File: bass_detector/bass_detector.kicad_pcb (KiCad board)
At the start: 2 copper layers, 65 x 65 mm, 27 parts, among them J1 AudioJack3, J2 Screw_Terminal_01x02, SW1 SW_SPST, U1 LM358

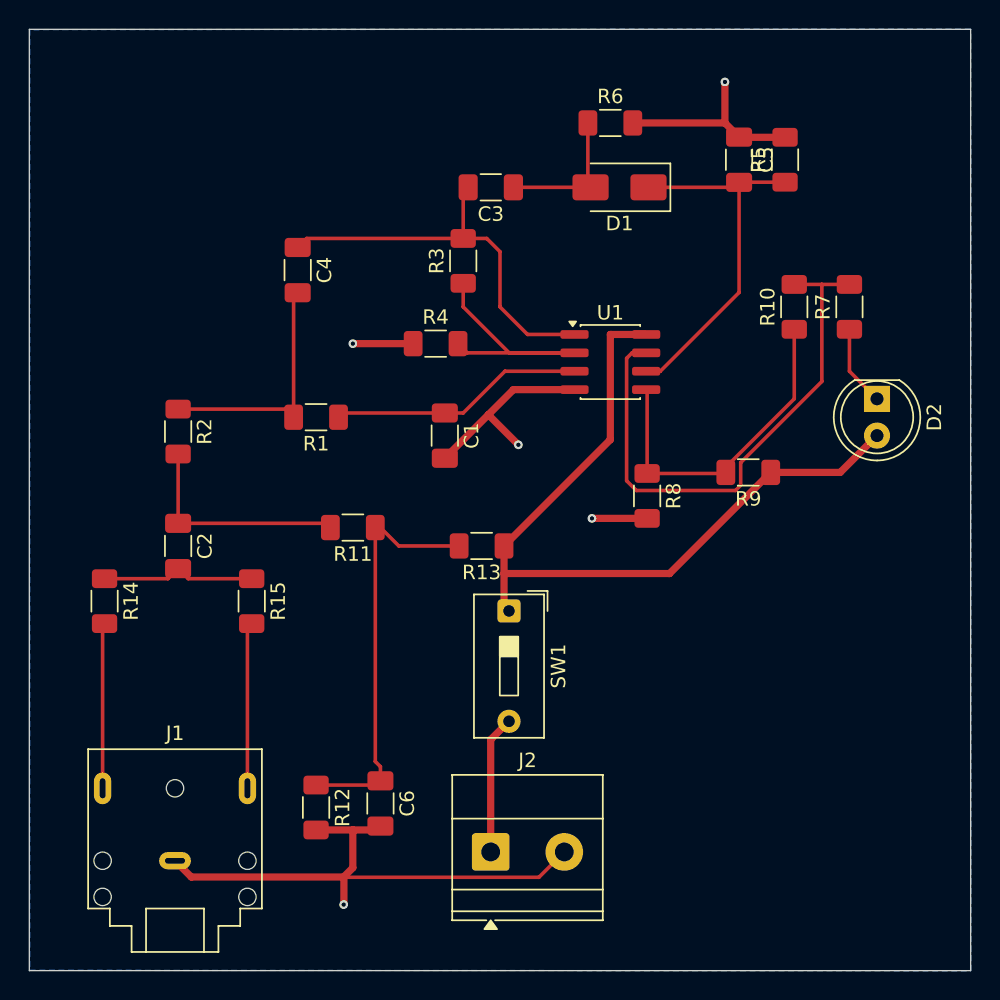
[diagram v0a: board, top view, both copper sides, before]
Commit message: made the pcb smaller, changed the language to be en only
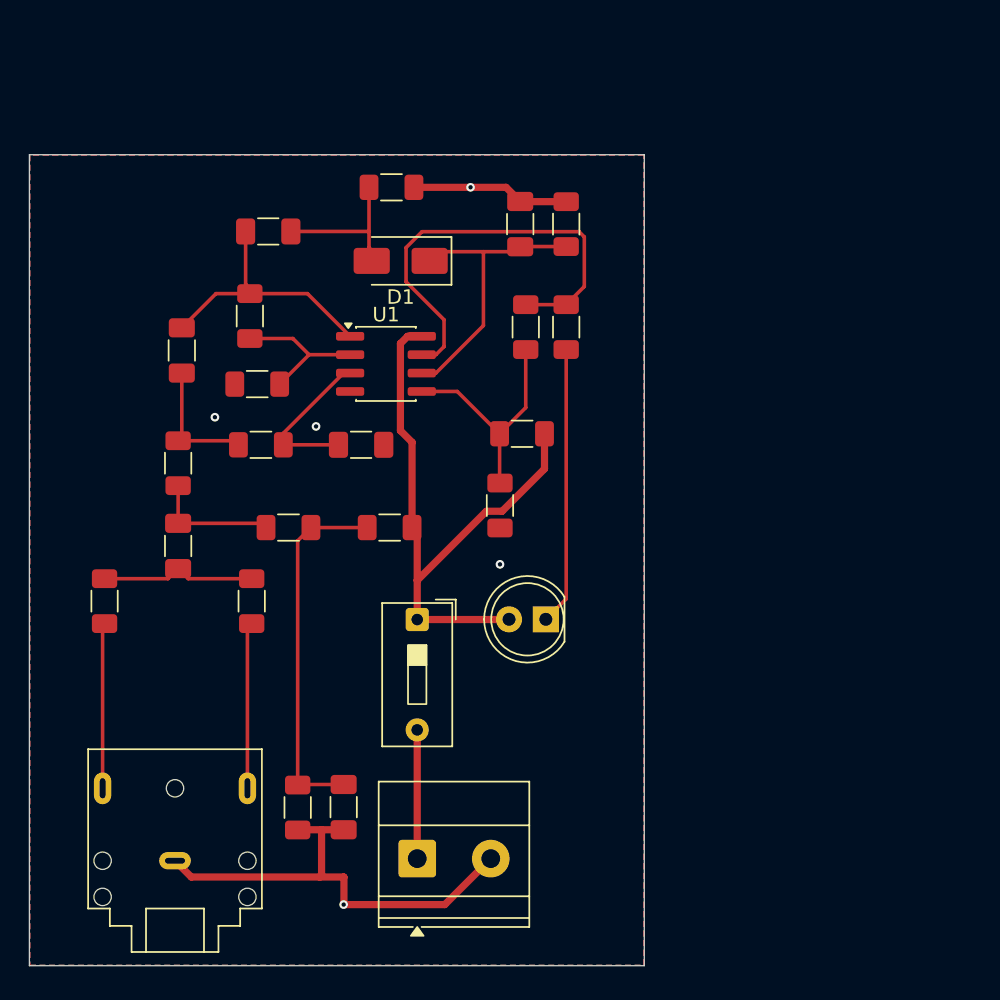
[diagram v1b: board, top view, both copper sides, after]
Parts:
- moved D2 27.5 mm to (153.7, 125.1), turned to 180 degrees
- moved R7 19.6 mm to (155.1, 104.9)
- moved R10 18.6 mm to (152.3, 104.9)
- moved D1 15.9 mm to (143.6, 100.3)
- moved R9 15.8 mm to (152.0, 112.3)
- moved C5 15.8 mm to (151.9, 97.8)
- moved R5 15.8 mm to (155.1, 97.8)
- moved R6 15.8 mm to (143.0, 95.2)
- moved C3 15.7 mm to (134.5, 98.3)
- moved U1 15.5 mm to (142.6, 107.4)
- moved R3 15.2 mm to (133.2, 104.1)
- moved R4 12.6 mm to (133.7, 108.8)
- moved R8 10.2 mm to (150.5, 117.2)
- moved C4 9.74 mm to (128.5, 106.5)
- moved R13 6.48 mm to (142.9, 118.7)
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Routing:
- net GND: track 73.6 -> 42.9 mm
- net Net-(D2-K): track 5.59 -> 19.2 mm
- net +9V: track 54.5 -> 42.4 mm
- net Net-(C3-Pad2): track 28.0 -> 18.7 mm
- net Net-(U1A--): track 18.9 -> 10.3 mm
- net Net-(C4-Pad2): track 17.3 -> 8.66 mm
- net Net-(R10-Pad2): track 38.3 -> 30.6 mm
- net Net-(U1A-+): track 17.6 -> 10.9 mm
- net Net-(C2-Pad1): track 15.4 -> 8.79 mm
- net Net-(U1B-+): track 23.1 -> 16.6 mm
- net Net-(D1-K): track 25.8 -> 20.3 mm
- net Net-(C6-Pad1): track 28.5 -> 25.2 mm
- net Net-(J2-Pin_1): track 9.54 -> 8.89 mm
- added copper zone on F.Cu, net GND
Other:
- board size 65 x 65 mm -> 42.5 x 56 mm

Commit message: adjustment to hysteresis and reference voltage, considering adding potentiometer to the open lab course, currently gonna stay
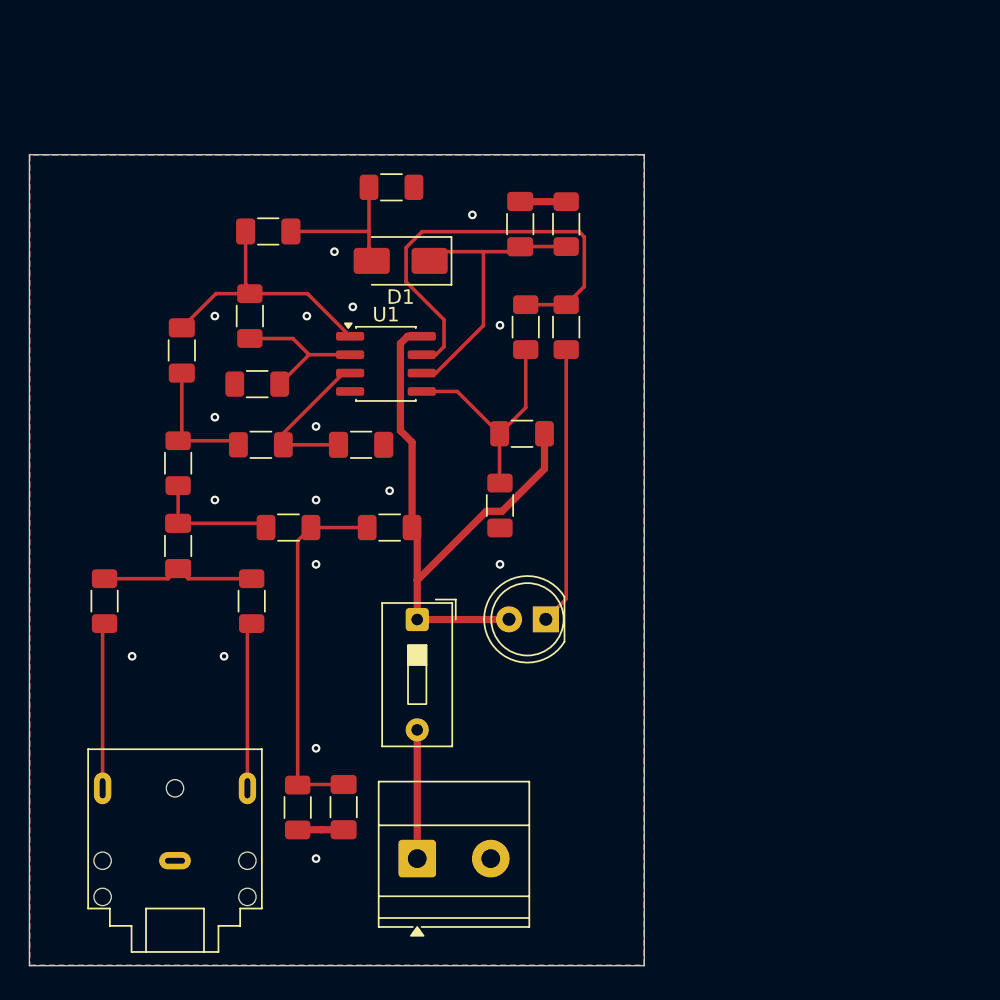
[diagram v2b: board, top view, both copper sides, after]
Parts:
- R10: value 430k -> 220k
- R8: value 3.3k -> 1k2
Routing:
- net GND: track 42.9 -> 6.36 mm, vias 5 -> 17
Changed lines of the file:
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@@
 			)
 		)
-		(property "Value" "430k"
+		(property "Value" "220k"
 			(at -2.794 -2.794 180)
 			(layer "F.Fab")
@@
 			)
 		)
-		(property "Value" "3.3k"
+		(property "Value" "1k2"
 			(at 0.127 -2.667 180)
 			(layer "F.Fab")
@@
 	)
 	(segment
-		(start 139.7 142.875)
-		(end 138.049 142.875)
-		(width 0.5)
-		(layer "F.Cu")
-		(net 1)
-	)
-	(segment
-		(start 149.86 141.605)
-		(end 146.685 144.78)
-		(width 0.5)
-		(layer "F.Cu")
-		(net 1)
-	)
-	(segment
 		(start 139.7 139.6115)
 		(end 138.176 139.6115)
@@
 	)
 	(segment
-		(start 138.176 142.748)
-		(end 138.049 142.875)
-		(width 0.5)
-		(layer "F.Cu")
-		(net 1)
-	)
-	(segment
 		(start 136.5385 139.6115)
 		(end 136.525 139.625)
@@
 	)
 	(segment
-		(start 138.176 139.6115)
-		(end 138.176 142.748)
+		(start 151.9045 96.24)
+		(end 151.892 96.2275)
 		(width 0.5)
 		(layer "F.Cu")
@@
 	)
 	(segment
-		(start 148.463 95.25)
-		(end 150.9145 95.25)
+		(start 155.067 96.24)
+		(end 151.9045 96.24)
 		(width 0.5)
 		(layer "F.Cu")
@@
 	)
 	(segment
-		(start 146.685 144.78)
-		(end 139.7 144.78)
+		(start 138.176 139.6115)
+		(end 136.5385 139.6115)
 		(width 0.5)
 		(layer "F.Cu")
 		(net 1)
 	)
-	(segment
-		(start 144.552 95.25)
-		(end 148.463 95.25)
-		(width 0.5)
-		(layer "F.Cu")
+	(via
+		(at 130.81 111.125)
+		(size 0.6)
+		(drill 0.3)
+		(layers "F.Cu" "B.Cu")
+		(free yes)
 		(net 1)
 	)
-	(segment
-		(start 150.9145 95.25)
-		(end 151.892 96.2275)
-		(width 0.5)
-		(layer "F.Cu")
+	(via
+		(at 137.795 133.985)
+		(size 0.6)
+		(drill 0.3)
+		(layers "F.Cu" "B.Cu")
+		(free yes)
 		(net 1)
 	)
-	(segment
-		(start 151.9045 96.24)
-		(end 151.892 96.2275)
-		(width 0.5)
-		(layer "F.Cu")
+	(via
+		(at 150.495 104.775)
+		(size 0.6)
+		(drill 0.3)
+		(layers "F.Cu" "B.Cu")
+		(free yes)
 		(net 1)
 	)
-	(segment
-		(start 155.067 96.24)
-		(end 151.9045 96.24)
-		(width 0.5)
-		(layer "F.Cu")
+	(via
+		(at 139.065 99.695)
+		(size 0.6)
+		(drill 0.3)
+		(layers "F.Cu" "B.Cu")
+		(free yes)
 		(net 1)
 	)
-	(segment
-		(start 139.7185 142.8935)
-		(end 139.7185 144.7615)
-		(width 0.5)
-		(layer "F.Cu")
+	(via
+		(at 142.875 116.205)
+		(size 0.6)
+		(drill 0.3)
+		(layers "F.Cu" "B.Cu")
+		(free yes)
 		(net 1)
 	)
-	(segment
-		(start 138.176 139.6115)
-		(end 136.5385 139.6115)
-		(width 0.5)
-		(layer "F.Cu")
+	(via
+		(at 131.445 127.635)
+		(size 0.6)
+		(drill 0.3)
+		(layers "F.Cu" "B.Cu")
+		(free yes)
 		(net 1)
 	)
-	(segment
-		(start 138.049 142.875)
-		(end 129.18 142.875)
-		(width 0.5)
-		(layer "F.Cu")
+	(via
+		(at 137.795 116.84)
+		(size 0.6)
+		(drill 0.3)
+		(layers "F.Cu" "B.Cu")
+		(free yes)
 		(net 1)
 	)
-	(segment
-		(start 129.18 142.875)
-		(end 128.055 141.75)
-		(width 0.5)
-		(layer "F.Cu")
+	(via
+		(at 137.795 111.76)
+		(size 0.6)
+		(drill 0.3)
+		(layers "F.Cu" "B.Cu")
+		(free yes)
 		(net 1)
 	)
-	(segment
-		(start 139.7185 142.8935)
-		(end 139.7 142.875)
-		(width 0.5)
-		(layer "F.Cu")
+	(via
+		(at 137.795 141.605)
+		(size 0.6)
+		(drill 0.3)
+		(layers "F.Cu" "B.Cu")
+		(free yes)
 		(net 1)
 	)
-	(segment
-		(start 139.7185 144.7615)
-		(end 139.7 144.78)
-		(width 0.5)
-		(layer "F.Cu")
+	(via
+		(at 148.59 97.155)
+		(size 0.6)
+		(drill 0.3)
+		(layers "F.Cu" "B.Cu")
+		(free yes)
 		(net 1)
 	)
 	(via
-		(at 130.81 111.125)
+		(at 130.81 116.84)
 		(size 0.6)
 		(drill 0.3)
@@
 	)
 	(via
-		(at 137.795 111.76)
+		(at 130.81 104.14)
 		(size 0.6)
 		(drill 0.3)
@@
 	)
 	(via
-		(at 148.463 95.25)
+		(at 125.095 127.635)
 		(size 0.6)
 		(drill 0.3)
 		(layers "F.Cu" "B.Cu")
+		(free yes)
 		(net 1)
 	)
@@
 	)
 	(via
-		(at 139.7 144.78)
+		(at 140.335 103.505)
+		(size 0.6)
+		(drill 0.3)
+		(layers "F.Cu" "B.Cu")
+		(free yes)
+		(net 1)
+	)
+	(via
+		(at 137.795 121.285)
 		(size 0.6)
 		(drill 0.3)
 		(layers "F.Cu" "B.Cu")
+		(free yes)
+		(net 1)
+	)
+	(via
+		(at 137.16 104.14)
+		(size 0.6)
+		(drill 0.3)
+		(layers "F.Cu" "B.Cu")
+		(free yes)
 		(net 1)
 	)
